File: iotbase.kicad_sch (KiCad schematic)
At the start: 13 parts, among them J1 USB_C_Receptacle_USB2.0, SW1 SW_Push, SW2 BOOT, U1 AMS1117-3.3, U2 STF202-22T1G, U3 ESP32-C3-WROOM-02

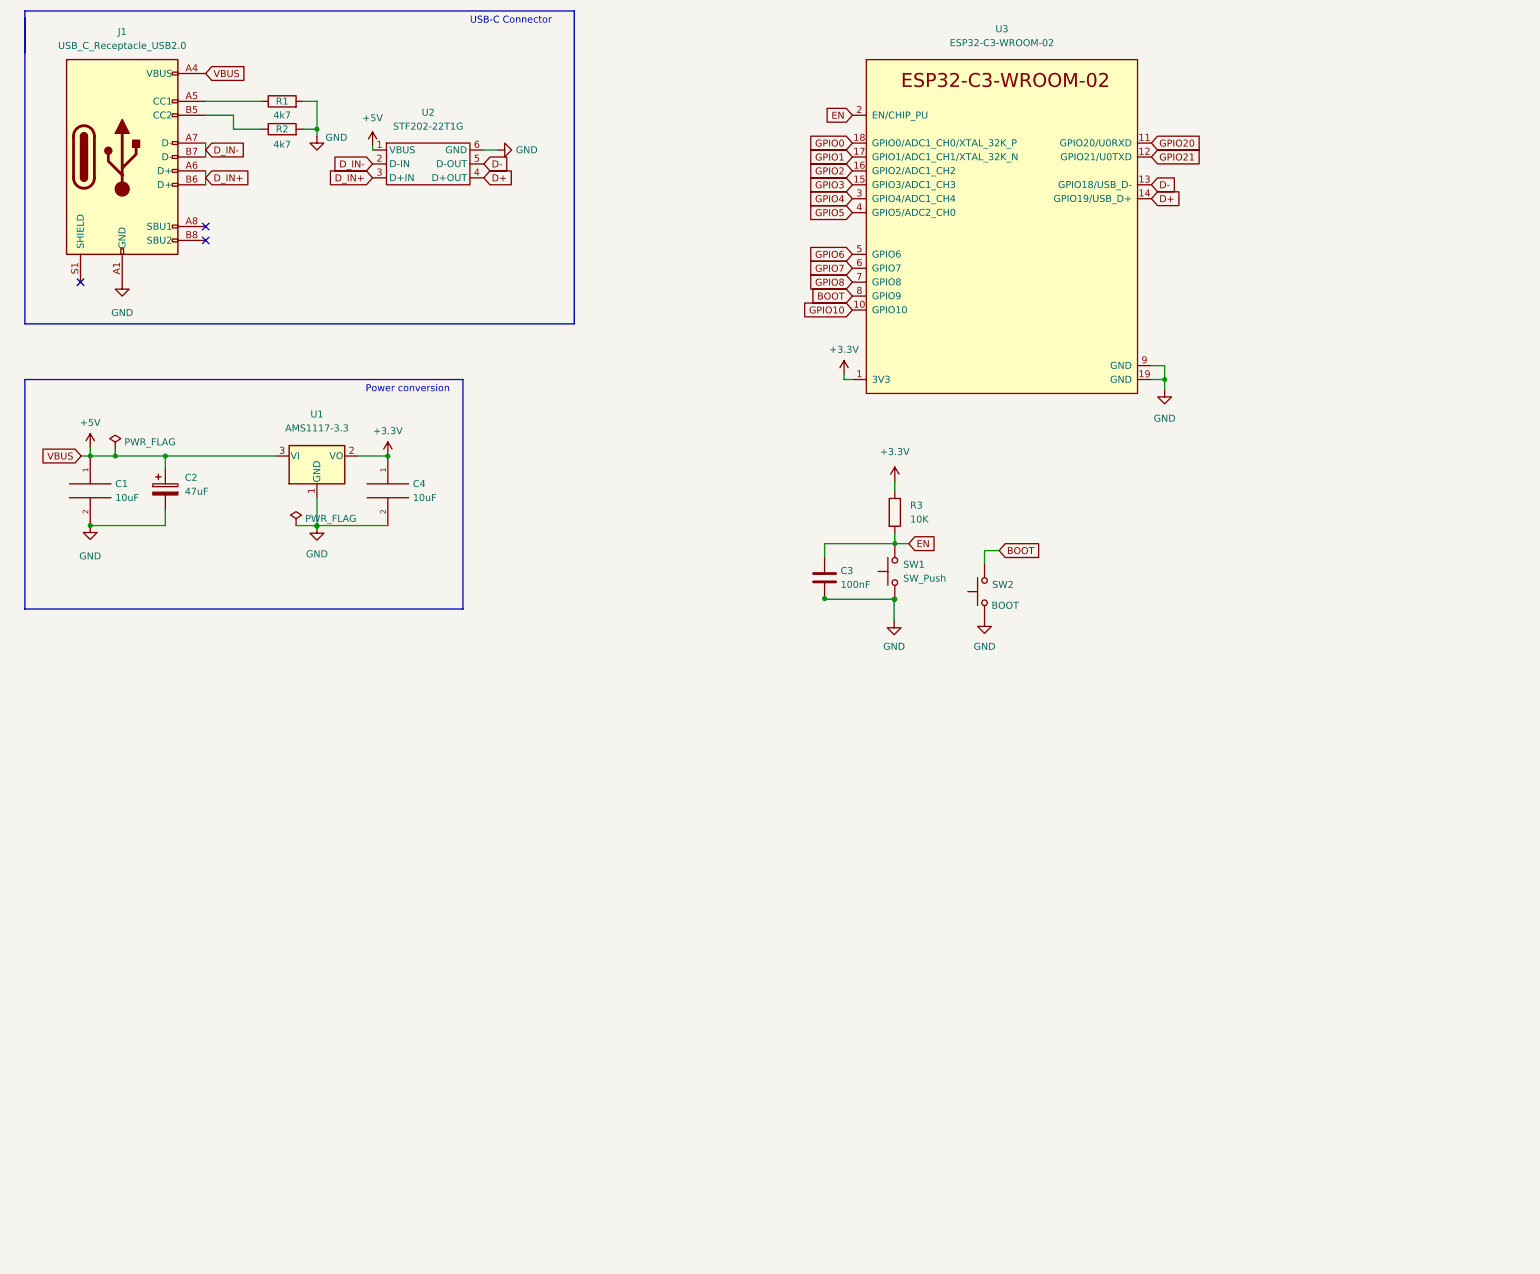
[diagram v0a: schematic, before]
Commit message: adds additionals sensors and connectors
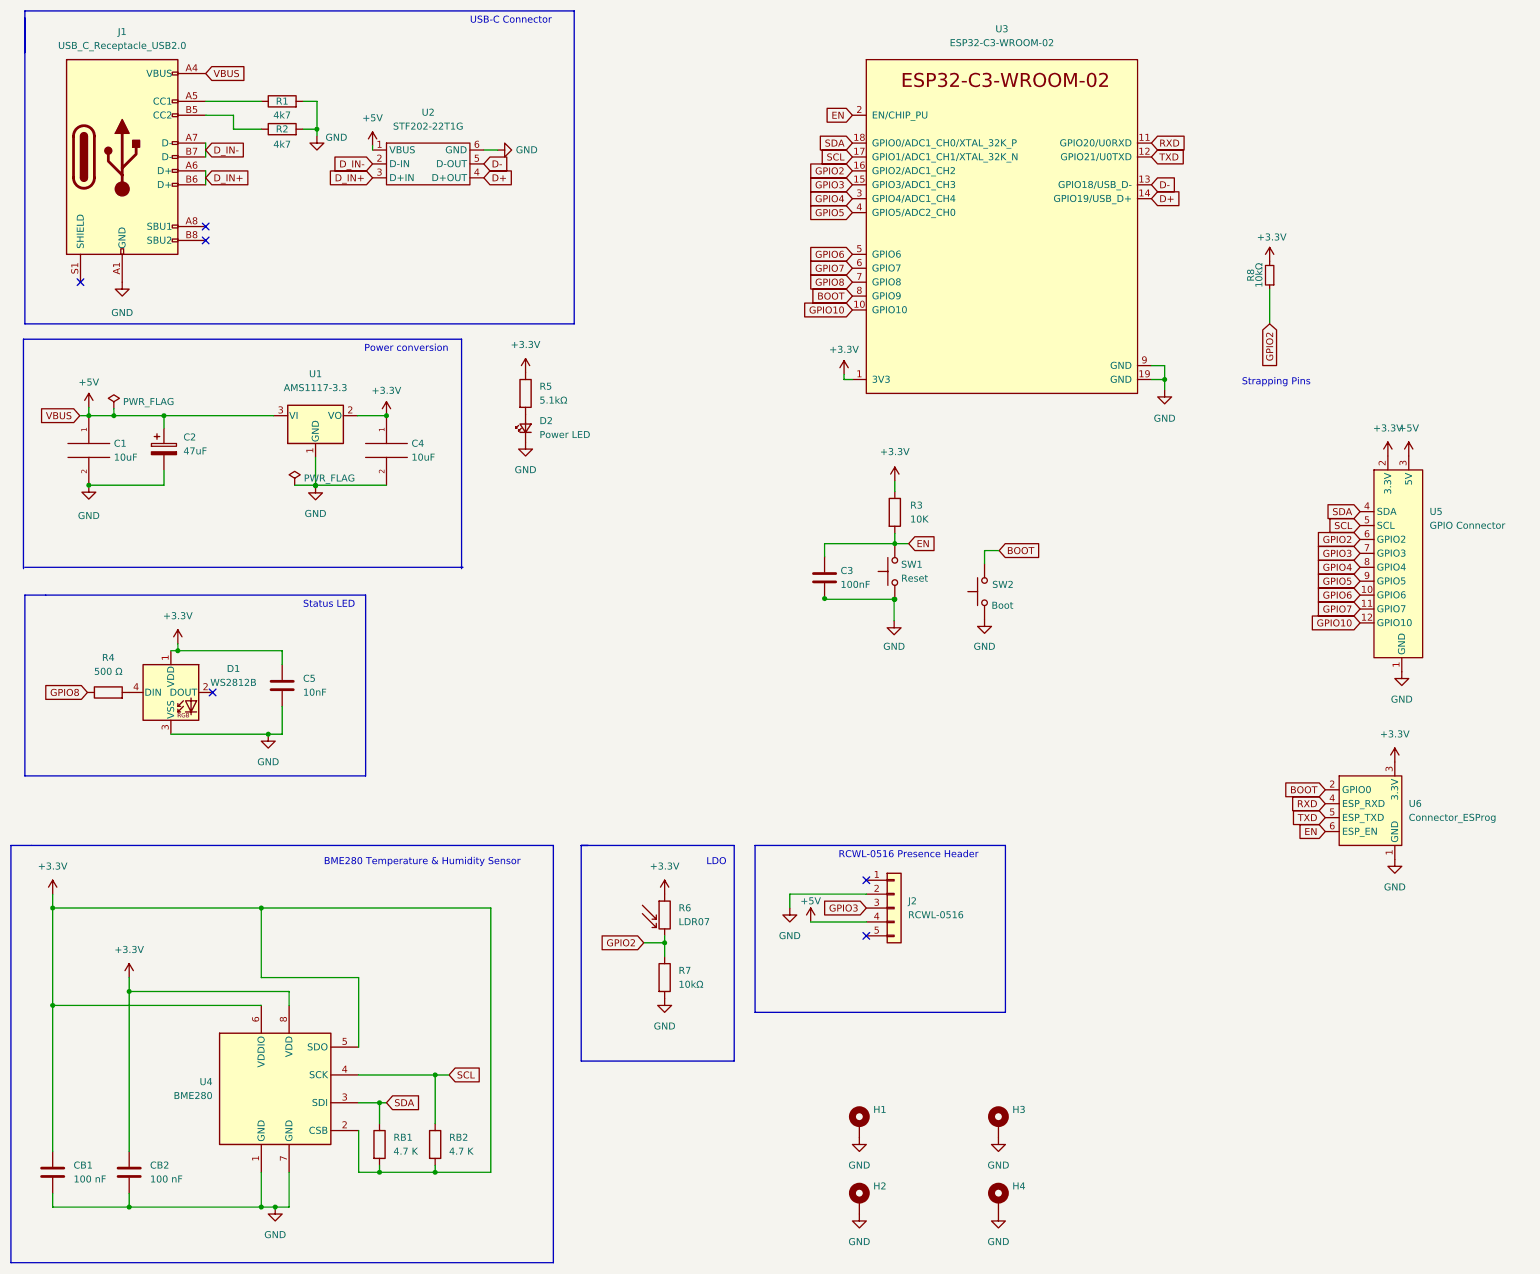
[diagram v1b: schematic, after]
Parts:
- added C5: 10nF, Resistor_SMD:R_0603_1608Metric, symbol Device:C
- added CB1, CB2: 100 nF, Capacitor_SMD:C_0603_1608Metric, symbol Device:C
- added D1: WS2812B, LED_SMD:LED_WS2812B_PLCC4_5.0x5.0mm_P3.2mm, symbol LED:WS2812B
- added D2: Power LED, LED_SMD:LED_0603_1608Metric, symbol Device:LED_Small
- added H1, H2, H3, H4: MountingHole_Pad, MountingHole:MountingHole_2.2mm_M2_Pad, symbol Mechanical:MountingHole_Pad
- added J2: RCWL-0516, Connector_PinHeader_2.54mm:PinHeader_1x05_P2.54mm_Vertical, symbol Connector_Generic:Conn_01x05
- added R4: 500 Ω, Resistor_SMD:R_0603_1608Metric, symbol Device:R
- added R5: 5.1kΩ, Resistor_SMD:R_0603_1608Metric, symbol Device:R
- added R6: LDR07, OptoDevice:R_LDR_5.1x4.3mm_P3.4mm_Vertical, symbol Sensor_Optical:LDR07
- added R7: 10kΩ, Resistor_SMD:R_0603_1608Metric, symbol Device:R
- added R8: 10kΩ, Resistor_SMD:R_0603_1608Metric, symbol Device:R_Small
- added RB1, RB2: 4.7 K, Resistor_SMD:R_0603_1608Metric, symbol Device:R
- added U4: BME280, Package_LGA:Bosch_LGA-8_2.5x2.5mm_P0.65mm_ClockwisePinNumbering, symbol Sensor:BME280
- added U5: GPIO Connector, 0_my_library:Connector_IoT_GPIO, symbol New_Library:Connector_IoT_GPIO
- added U6: Connector_ESProg, Connector:Tag-Connect_TC2030-IDC-FP_2x03_P1.27mm_Vertical, symbol New_Library:Connector_ESProg
- SW1: value SW_Push -> Reset
- SW2: value BOOT -> Boot
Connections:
- net +3V3: now also C5.1, CB1.1, CB2.1, D1.1 (VDD), R5.1, R6.1, R8.2, RB1.2, RB2.2, U4.2 (CSB), U4.5 (SDO), U4.6 (VDDIO), U4.8 (VDD), U5.2 (3.3V), U6.3 (3.3V)
- net +5V: now also J2.4 (Pin_4), U5.3 (5V)
- net BOOT: now also U6.2 (GPIO0)
- net EN: now also U6.6 (ESP_EN)
- net GND: now also C5.2, CB1.2, CB2.2, D1.3 (VSS), D2.1 (K), H1.1, H2.1, H3.1, H4.1, J2.2 (Pin_2), R7.2, U4.1 (GND), U4.7 (GND), U5.1 (GND), U6.1 (GND)
- net GPIO10: now also U5.12 (GPIO10)
- net GPIO2: now also R6.2, R7.1, R8.1, U5.6 (GPIO2)
- net GPIO3: now also J2.3 (Pin_3), U5.7 (GPIO3)
- net GPIO4: now also U5.8 (GPIO4)
- net GPIO5: now also U5.9 (GPIO5)
- net GPIO6: now also U5.10 (GPIO6)
- net GPIO7: now also U5.11 (GPIO7)
- net GPIO8: now also R4.1
- net GPIO0 renamed SDA
- net SDA: now also RB1.1, U4.3 (SDI), U5.4 (SDA)
- net GPIO1 renamed SCL
- net SCL: now also RB2.1, U4.4 (SCK), U5.5 (SCL)
- net GPIO20 renamed RXD
- net RXD: now also U6.4 (ESP_RXD)
- net GPIO21 renamed TXD
- net TXD: now also U6.5 (ESP_TXD)
- new net: D2.2 (A), R5.2
- new net: D1.4 (DIN), R4.2
- no-connect marks 3 -> 6
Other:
- note added: "BME280 Temperature & Humidity Sensor"
- note added: "LDO"
- note added: "RCWL-0516 Presence Header"
- note added: "Status LED"
- note added: "Strapping Pins"
- moved on the sheet: C1, C2, C4, U1
